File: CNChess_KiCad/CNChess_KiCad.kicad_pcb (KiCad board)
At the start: 2 copper layers, 86.7 x 53.6 mm, 36 parts, among them J1 Servomotor, J2 Barrel_Jack, J3 Motor1, J4 Motor2, J5 Fan, SW1 LSW1, SW2 LSW2, SW3 OOSW, U1 ESP32C3, U2 Power_Regulator

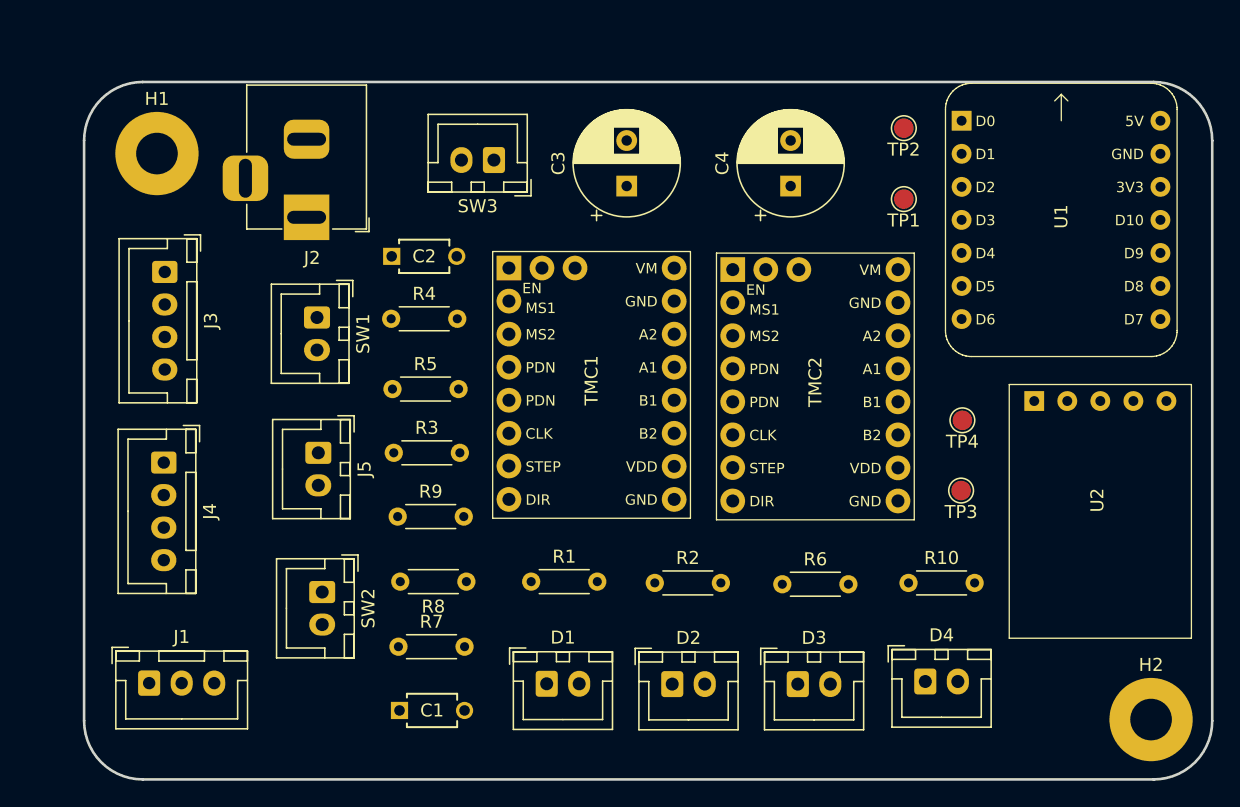
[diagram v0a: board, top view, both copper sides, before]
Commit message: PCB tracks + remise tableau de bord 1
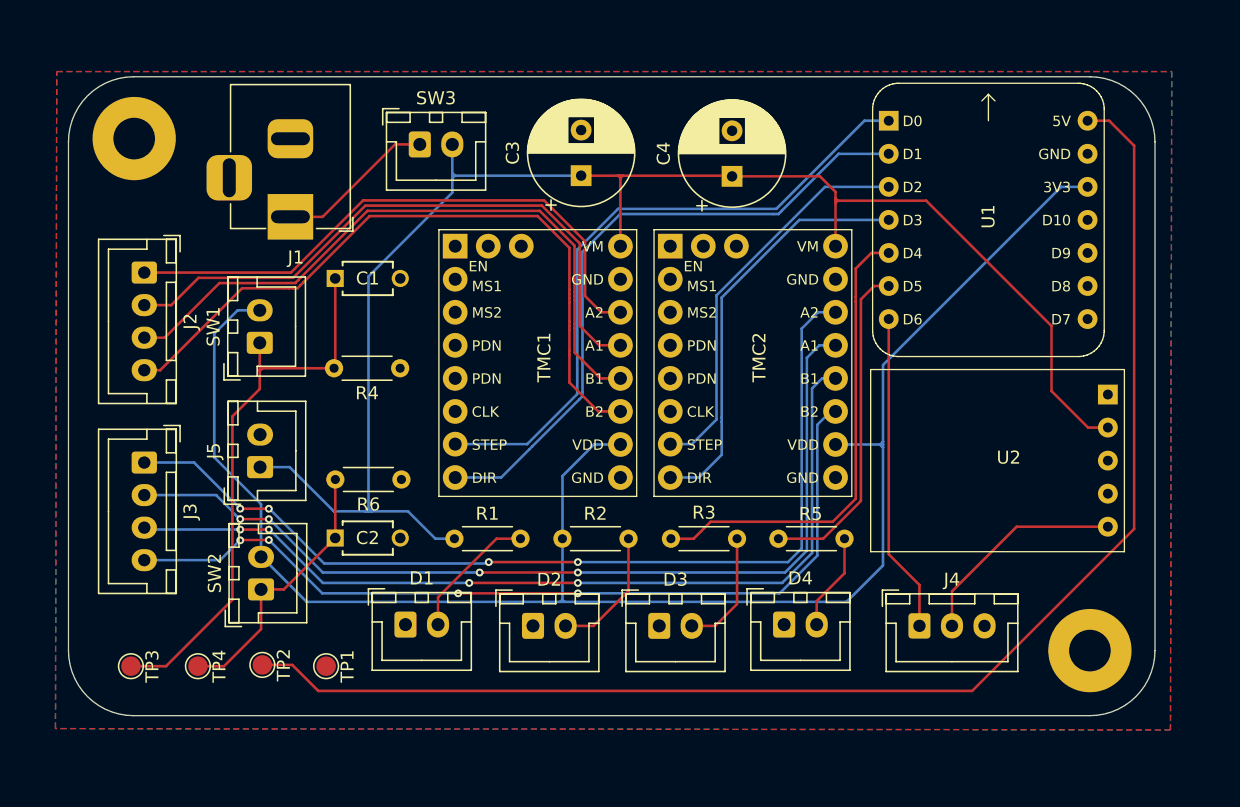
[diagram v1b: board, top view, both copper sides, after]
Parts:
- removed R10: 1k, Resistor_THT:R_Axial_DIN0204_L3.6mm_D1.6mm_P5.08mm_Horizontal
- removed R7: 470, Resistor_THT:R_Axial_DIN0204_L3.6mm_D1.6mm_P5.08mm_Horizontal
- removed R8: 180, Resistor_THT:R_Axial_DIN0204_L3.6mm_D1.6mm_P5.08mm_Horizontal
- removed R9: 47k, Resistor_THT:R_Axial_DIN0204_L3.6mm_D1.6mm_P5.08mm_Horizontal
- D2: value 5V LED -> 3V3 LED
- J1: value Servomotor -> Barrel_Jack; footprint Connector_JST:JST_XH_B3B-XH-A_1x03_P2.50mm_Vertical -> CNChess_footprints:BarrelJack_Horizontal
- J2: value Barrel_Jack -> Motor1; footprint CNChess_footprints:BarrelJack_Horizontal -> Connector_JST:JST_XH_B4B-XH-A_1x04_P2.50mm_Vertical
- J3: value Motor1 -> Motor2
- J4: value Motor2 -> Servomotor; footprint Connector_JST:JST_XH_B4B-XH-A_1x04_P2.50mm_Vertical -> Connector_JST:JST_XH_B3B-XH-A_1x03_P2.50mm_Vertical
- R2: value 300 -> 270
- R3: value 47k -> 270
- R4: value 470 -> 47k
- R5: value 180 -> 270
- R6: value 1k -> 47k
- moved TP3 65.2 mm to (118.7, 124.8), turned to -90 degrees
- moved TP2 64.3 mm to (128.8, 124.7), turned to -90 degrees
- moved TP4 61.7 mm to (123.8, 124.8), turned to -90 degrees
- moved J4 59.4 mm to (179.3, 121.7), turned to 0 degrees
- moved TP1 57.1 mm to (133.7, 124.8), turned to -90 degrees
- moved J1 37.4 mm to (131.0, 90.3), turned to -90 degrees
- moved R5 36.6 mm to (173.5, 115.0), turned to 180 degrees
- moved C1 33.6 mm to (134.4, 95.0)
- moved R6 30.4 mm to (139.5, 110.5), turned to 180 degrees
- moved R3 27.2 mm to (165.3, 115.0), turned to 180 degrees
- moved C2 22.1 mm to (134.4, 115.0)
- moved J3 14.7 mm to (119.7, 109.2)
- moved J2 13.2 mm to (119.7, 94.5)
- moved D1 11.8 mm to (139.8, 121.6)
- moved D4 11.7 mm to (168.9, 121.6)
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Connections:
- J1 pad 1: SERVO -> Net-(SW3-A)
- J1 pad 2: Net-(J1-Pin_2) -> GND
- J1 pad 3: GND -> (no net)
- J2 pad 1: Net-(SW3-A) -> Net-(J2-Pin_1)
- J2 pad 2: GND -> Net-(J2-Pin_2)
- J2 pad 3: (no net) -> Net-(J2-Pin_3)
- J4 pad 1: Net-(J4-Pin_1) -> SERVO
- J4 pad 3: Net-(J4-Pin_3) -> GND
- R2 pad 1: +5V -> +3V3
- R3 pad 1: SW1 -> Net-(D3-A)
- R3 pad 2: Net-(R3-Pad2) -> SW1
- R4 pad 1: Net-(R3-Pad2) -> GND
- R4 pad 2: Net-(R4-Pad2) -> SW1
- R5 pad 1: Net-(R3-Pad2) -> Net-(D4-A)
- R5 pad 2: GND -> SW2
- R6 pad 1: Net-(R4-Pad2) -> GND
- R6 pad 2: Net-(D3-A) -> SW2
- SW1 pad 1: Net-(R4-Pad2) -> SW1
- SW1 pad 2: +12V -> +3V3
- SW2 pad 1: Net-(R10-Pad1) -> SW2
- SW2 pad 2: +12V -> +3V3
- TMC1 pad 10: +5V -> +3V3
- TMC1 pad 11: Net-(J3-Pin_4) -> Net-(J2-Pin_4)
- TMC1 pad 12: Net-(J3-Pin_3) -> Net-(J2-Pin_3)
- TMC1 pad 13: Net-(J3-Pin_2) -> Net-(J2-Pin_2)
- TMC1 pad 14: Net-(J3-Pin_1) -> Net-(J2-Pin_1)
- TMC2 pad 10: +5V -> +3V3
- TMC2 pad 11: Net-(J4-Pin_4) -> Net-(J3-Pin_4)
- TMC2 pad 12: Net-(J4-Pin_3) -> Net-(J3-Pin_3)
- TMC2 pad 13: Net-(J4-Pin_2) -> Net-(J3-Pin_2)
- TMC2 pad 14: Net-(J4-Pin_1) -> Net-(J3-Pin_1)
- U1 pad 12: unconnected-(U1-3V3-Pad12) -> +3V3
- U2 pad 1: +12V -> unconnected-(U2-EN-Pad1)
- U2 pad 5: Net-(J1-Pin_2) -> Net-(J4-Pin_2)
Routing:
- net +3V3: track 0.00 -> 129.8 mm
- net +12V: track 0.00 -> 121.1 mm
- net +5V: track 0.00 -> 106.8 mm
- net SW1: track 0.00 -> 79.8 mm
- net Net-(J3-Pin_1): track 0.00 -> 74.2 mm, vias 0 -> 4
- net Net-(J3-Pin_2): track 0.00 -> 71.5 mm, vias 0 -> 4
- net Net-(J3-Pin_3): track 0.00 -> 68.8 mm, vias 0 -> 4
- net Net-(J3-Pin_4): track 0.00 -> 67.1 mm, vias 0 -> 4
- net Net-(J2-Pin_4): track 0.00 -> 53.8 mm
- net Net-(J2-Pin_3): track 0.00 -> 50.8 mm
- net DIR1: track 0.00 -> 50.1 mm
- net STEP1: track 0.00 -> 50.1 mm
- net Net-(J2-Pin_2): track 0.00 -> 47.9 mm
- net SW2: track 0.00 -> 46.6 mm
- net Net-(J2-Pin_1): track 0.00 -> 44.9 mm
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- added copper zone on B.Cu, net GND
- added copper zone on F.Cu, net GND
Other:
- board size 86.7 x 53.6 mm -> 83.5 x 49.1 mm

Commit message: ajout des modèles 3d et terminé V1 du PCB
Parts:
- C3, C4: footprint Capacitor_THT:CP_Radial_D8.0mm_P3.50mm -> Capacitor_THT:CP_Radial_D10.0mm_P5.00mm
- moved J1 8.04 mm to (129.5, 82.3), turned to 90 degrees
- moved SW3 2.40 mm to (140.9, 82.3)
- moved C4 1.40 mm to (166.3, 87.1)
- moved U1 1.10 mm to (184.6, 89.4)
- moved H1 1.08 mm to (118.7, 83.2)
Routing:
- net SW1: track 79.8 -> 119.3 mm
- net SW2: track 46.6 -> 84.5 mm, vias 0 -> 1
- net +12V: track 121.1 -> 138.4 mm
- net GND: track 0.00 -> 5.95 mm, vias 0 -> 3
- net Net-(SW3-A): track 12.7 -> 15.5 mm
- net SERVO: track 24.6 -> 25.7 mm
- net +3V3: track 129.8 -> 130.5 mm
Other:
- board size 83.5 x 49.1 mm -> 83.7 x 50.9 mm
